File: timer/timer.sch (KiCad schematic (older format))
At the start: 31 parts, among them P1 Keypad, P2 Display, P3 Handset, P4 PWR, P5 Hook, P6 Encoder, P7 SPKR, Q1 S8050, Q2 PN2222A, U1 74HC595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

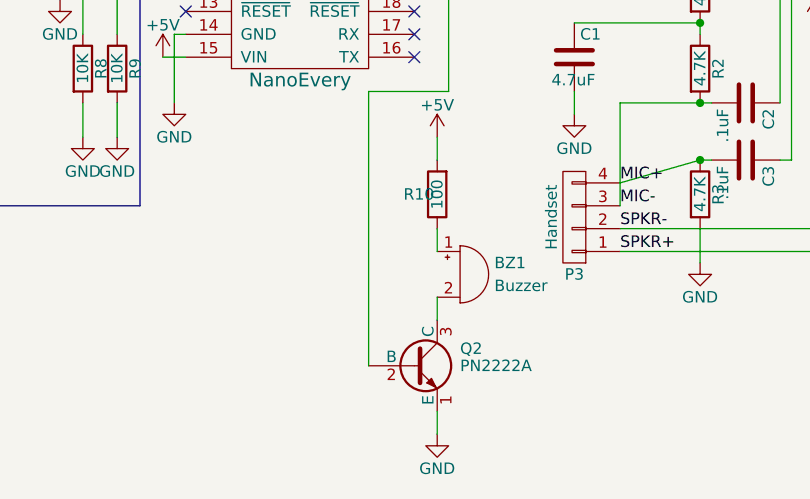
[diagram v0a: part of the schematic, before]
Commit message: added diode D1 to schematic, fixed bug with digitalRead
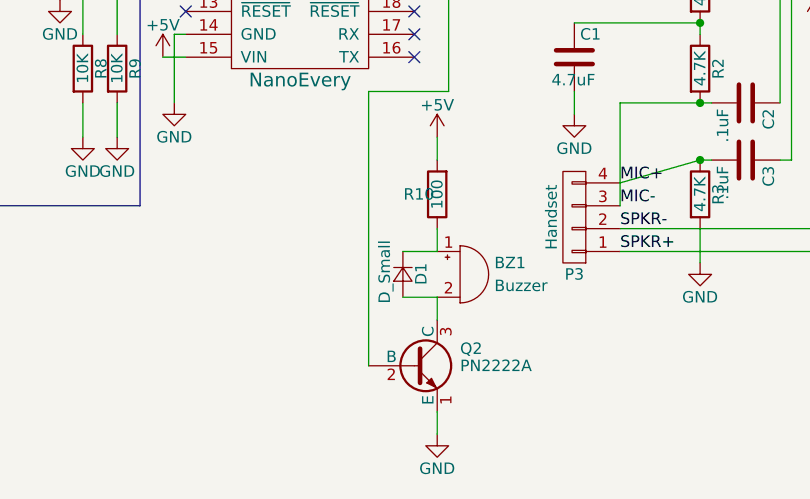
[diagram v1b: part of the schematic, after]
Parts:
- added D1: D_Small, symbol D_Small
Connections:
- net at BZ1.1 (-), R10.1: now also D1.1 (K)
- net at BZ1.2 (+), Q2.3 (C): now also D1.2 (A)
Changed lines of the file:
@@
 $EndComp
 $Comp
-L GND #PWR01
+L GND #PWR2
 U 1 1 5E1F1F7E
 P 3050 2500
-F 0 "#PWR01" H 3050 2250 50  0001 C CNN
+F 0 "#PWR2" H 3050 2250 50  0001 C CNN
 F 1 "GND" H 3050 2350 50  0000 C CNN
 F 2 "" H 3050 2500 50  0000 C CNN
@@
 $EndComp
 $Comp
-L +5V #PWR02
+L +5V #PWR1
 U 1 1 5E1F2C3E
 P 3050 2050
-F 0 "#PWR02" H 3050 1900 50  0001 C CNN
+F 0 "#PWR1" H 3050 1900 50  0001 C CNN
 F 1 "+5V" H 3050 2190 50  0000 C CNN
 F 2 "" H 3050 2050 50  0000 C CNN
@@
 $EndComp
 $Comp
-L GND #PWR03
+L GND #PWR28
 U 1 1 5E1FC8DD
 P 9300 3600
-F 0 "#PWR03" H 9300 3350 50  0001 C CNN
+F 0 "#PWR28" H 9300 3350 50  0001 C CNN
 F 1 "GND" H 9300 3450 50  0000 C CNN
 F 2 "" H 9300 3600 50  0000 C CNN
@@
 $EndComp
 $Comp
-L +5V #PWR04
+L +5V #PWR25
 U 1 1 5E1FC95C
 P 7900 2600
-F 0 "#PWR04" H 7900 2450 50  0001 C CNN
+F 0 "#PWR25" H 7900 2450 50  0001 C CNN
 F 1 "+5V" H 7900 2740 50  0000 C CNN
 F 2 "" H 7900 2600 50  0000 C CNN
@@
 $EndComp
 $Comp
-L +5V #PWR05
+L +5V #PWR23
 U 1 1 5E1FC9C9
 P 7500 4050
-F 0 "#PWR05" H 7500 3900 50  0001 C CNN
+F 0 "#PWR23" H 7500 3900 50  0001 C CNN
 F 1 "+5V" H 7500 4190 50  0000 C CNN
 F 2 "" H 7500 4050 50  0000 C CNN
@@
 $EndComp
 $Comp
-L GND #PWR06
+L GND #PWR26
 U 1 1 5E1FCA32
 P 7900 4500
-F 0 "#PWR06" H 7900 4250 50  0001 C CNN
+F 0 "#PWR26" H 7900 4250 50  0001 C CNN
 F 1 "GND" H 7900 4350 50  0000 C CNN
 F 2 "" H 7900 4500 50  0000 C CNN
@@
 $EndComp
 $Comp
-L GND #PWR07
+L GND #PWR24
 U 1 1 5E1FCA50
 P 7700 4400
-F 0 "#PWR07" H 7700 4150 50  0001 C CNN
+F 0 "#PWR24" H 7700 4150 50  0001 C CNN
 F 1 "GND" H 7700 4250 50  0000 C CNN
 F 2 "" H 7700 4400 50  0000 C CNN
@@
 $EndComp
 $Comp
-L GND #PWR08
+L GND #PWR30
 U 1 1 5E1FCA6E
 P 9350 4000
-F 0 "#PWR08" H 9350 3750 50  0001 C CNN
+F 0 "#PWR30" H 9350 3750 50  0001 C CNN
 F 1 "GND" H 9350 3850 50  0000 C CNN
 F 2 "" H 9350 4000 50  0000 C CNN
@@
 $EndComp
 $Comp
-L GND #PWR09
+L GND #PWR29
 U 1 1 5E1FCA8C
 P 9350 2800
-F 0 "#PWR09" H 9350 2550 50  0001 C CNN
+F 0 "#PWR29" H 9350 2550 50  0001 C CNN
 F 1 "GND" H 9350 2650 50  0000 C CNN
 F 2 "" H 9350 2800 50  0000 C CNN
@@
 $EndComp
 $Comp
-L GND #PWR010
+L GND #PWR22
 U 1 1 5E21BE44
 P 7500 2900
-F 0 "#PWR010" H 7500 2650 50  0001 C CNN
+F 0 "#PWR22" H 7500 2650 50  0001 C CNN
 F 1 "GND" H 7500 2750 50  0000 C CNN
 F 2 "" H 7500 2900 50  0000 C CNN
@@
 $EndComp
 $Comp
-L GND #PWR011
+L GND #PWR31
 U 1 1 5E21C2BB
 P 9600 3500
-F 0 "#PWR011" H 9600 3250 50  0001 C CNN
+F 0 "#PWR31" H 9600 3250 50  0001 C CNN
 F 1 "GND" H 9600 3350 50  0000 C CNN
 F 2 "" H 9600 3500 50  0000 C CNN
@@
 $EndComp
 $Comp
-L GND #PWR012
+L GND #PWR32
 U 1 1 5E21C486
 P 9750 3850
-F 0 "#PWR012" H 9750 3600 50  0001 C CNN
+F 0 "#PWR32" H 9750 3600 50  0001 C CNN
 F 1 "GND" H 9750 3700 50  0000 C CNN
 F 2 "" H 9750 3850 50  0000 C CNN
@@
 $EndComp
 $Comp
-L +5V #PWR013
+L +5V #PWR27
 U 1 1 5E254DF9
 P 9150 3450
-F 0 "#PWR013" H 9150 3300 50  0001 C CNN
+F 0 "#PWR27" H 9150 3300 50  0001 C CNN
 F 1 "+5V" H 9150 3590 50  0000 C CNN
 F 2 "" H 9150 3450 50  0000 C CNN
@@
 $EndComp
 $Comp
-L +5V #PWR014
+L +5V #PWR20
 U 1 1 5E255EBE
 P 7000 3650
-F 0 "#PWR014" H 7000 3500 50  0001 C CNN
+F 0 "#PWR20" H 7000 3500 50  0001 C CNN
 F 1 "+5V" H 7000 3790 50  0000 C CNN
 F 2 "" H 7000 3650 50  0000 C CNN
@@
 $EndComp
 $Comp
-L GND #PWR015
+L GND #PWR21
 U 1 1 5E255FFF
 P 7000 5100
-F 0 "#PWR015" H 7000 4850 50  0001 C CNN
+F 0 "#PWR21" H 7000 4850 50  0001 C CNN
 F 1 "GND" H 7000 4950 50  0000 C CNN
 F 2 "" H 7000 5100 50  0000 C CNN
@@
 $EndComp
 $Comp
-L GND #PWR016
+L GND #PWR33
 U 1 1 5E257195
 P 9950 4900
-F 0 "#PWR016" H 9950 4650 50  0001 C CNN
+F 0 "#PWR33" H 9950 4650 50  0001 C CNN
 F 1 "GND" H 9950 4750 50  0000 C CNN
 F 2 "" H 9950 4900 50  0000 C CNN
@@
 $EndComp
 $Comp
-L +5V #PWR017
+L +5V #PWR34
 U 1 1 5E257AF2
 P 10300 4150
-F 0 "#PWR017" H 10300 4000 50  0001 C CNN
+F 0 "#PWR34" H 10300 4000 50  0001 C CNN
 F 1 "+5V" H 10300 4290 50  0000 C CNN
 F 2 "" H 10300 4150 50  0000 C CNN
@@
 $EndComp
 $Comp
-L GND #PWR018
+L GND #PWR18
 U 1 1 5E25949D
 P 6450 4450
-F 0 "#PWR018" H 6450 4200 50  0001 C CNN
+F 0 "#PWR18" H 6450 4200 50  0001 C CNN
 F 1 "GND" H 6450 4300 50  0000 C CNN
 F 2 "" H 6450 4450 50  0000 C CNN
@@
 $EndComp
 $Comp
-L +5V #PWR020
+L +5V #PWR15
 U 1 1 5E25EB56
 P 5800 2150
-F 0 "#PWR020" H 5800 2000 50  0001 C CNN
+F 0 "#PWR15" H 5800 2000 50  0001 C CNN
 F 1 "+5V" H 5800 2290 50  0000 C CNN
 F 2 "" H 5800 2150 50  0000 C CNN
@@
 $EndComp
 $Comp
-L GND #PWR021
+L GND #PWR19
 U 1 1 5E25EC43
 P 6600 2150
-F 0 "#PWR021" H 6600 1900 50  0001 C CNN
+F 0 "#PWR19" H 6600 1900 50  0001 C CNN
 F 1 "GND" H 6600 2000 50  0000 C CNN
 F 2 "" H 6600 2150 50  0000 C CNN
@@
 $EndComp
 $Comp
-L +5V #PWR022
+L +5V #PWR11
 U 1 1 5E25F4BB
 P 4650 4200
-F 0 "#PWR022" H 4650 4050 50  0001 C CNN
+F 0 "#PWR11" H 4650 4050 50  0001 C CNN
 F 1 "+5V" H 4650 4340 50  0000 C CNN
 F 2 "" H 4650 4200 50  0000 C CNN
@@
 $EndComp
 $Comp
-L GND #PWR023
+L GND #PWR12
 U 1 1 5E25F508
 P 4700 4400
-F 0 "#PWR023" H 4700 4150 50  0001 C CNN
+F 0 "#PWR12" H 4700 4150 50  0001 C CNN
 F 1 "GND" H 4700 4250 50  0000 C CNN
 F 2 "" H 4700 4400 50  0000 C CNN
@@
 $EndComp
 $Comp
-L GND #PWR024
+L GND #PWR10
 U 1 1 5E25F9A8
 P 4500 2200
-F 0 "#PWR024" H 4500 1950 50  0001 C CNN
+F 0 "#PWR10" H 4500 1950 50  0001 C CNN
 F 1 "GND" H 4500 2050 50  0000 C CNN
 F 2 "" H 4500 2200 50  0000 C CNN
@@
 $EndComp
 $Comp
-L +5V #PWR025
+L +5V #PWR13
 U 1 1 5E25F9F8
 P 4800 2150
-F 0 "#PWR025" H 4800 2000 50  0001 C CNN
+F 0 "#PWR13" H 4800 2000 50  0001 C CNN
 F 1 "+5V" H 4800 2290 50  0000 C CNN
 F 2 "" H 4800 2150 50  0000 C CNN
@@
 	6300 3300 6300 2150
 $Comp
-L GND #PWR026
+L GND #PWR5
 U 1 1 5E260E32
 P 3850 3350
-F 0 "#PWR026" H 3850 3100 50  0001 C CNN
+F 0 "#PWR5" H 3850 3100 50  0001 C CNN
 F 1 "GND" H 3850 3200 50  0000 C CNN
 F 2 "" H 3850 3350 50  0000 C CNN
@@
 NoConn ~ 7900 2900
 $Comp
-L +5V #PWR027
+L +5V #PWR3
 U 1 1 5E27D47A
 P 3200 4200
-F 0 "#PWR027" H 3200 4050 50  0001 C CNN
+F 0 "#PWR3" H 3200 4050 50  0001 C CNN
 F 1 "+5V" H 3200 4340 50  0000 C CNN
 F 2 "" H 3200 4200 50  0000 C CNN
@@
 	3000 4200 3000 4050
 $Comp
-L GND #PWR028
+L GND #PWR4
 U 1 1 5E27DD28
 P 3550 2900
-F 0 "#PWR028" H 3550 2650 50  0001 C CNN
+F 0 "#PWR4" H 3550 2650 50  0001 C CNN
 F 1 "GND" H 3550 2750 50  0000 C CNN
 F 2 "" H 3550 2900 50  0000 C CNN
@@
 	4200 3400 4200 3500
 $Comp
-L GND #PWR029
+L GND #PWR6
 U 1 1 5E2CB89E
 P 4050 3750
-F 0 "#PWR029" H 4050 3500 50  0001 C CNN
+F 0 "#PWR6" H 4050 3500 50  0001 C CNN
 F 1 "GND" H 4050 3600 50  0000 C CNN
 F 2 "" H 4050 3750 50  0000 C CNN
@@
 $EndComp
 $Comp
-L GND #PWR030
+L GND #PWR7
 U 1 1 5E2CB900
 P 4200 3950
-F 0 "#PWR030" H 4200 3700 50  0001 C CNN
+F 0 "#PWR7" H 4200 3700 50  0001 C CNN
 F 1 "GND" H 4200 3800 50  0000 C CNN
 F 2 "" H 4200 3950 50  0000 C CNN
@@
 $EndComp
 $Comp
-L GND #PWR031
+L GND #PWR8
 U 1 1 5E2CB962
 P 4300 4550
-F 0 "#PWR031" H 4300 4300 50  0001 C CNN
+F 0 "#PWR8" H 4300 4300 50  0001 C CNN
 F 1 "GND" H 4300 4400 50  0000 C CNN
 F 2 "" H 4300 4550 50  0000 C CNN
@@
 $EndComp
 $Comp
-L GND #PWR032
+L GND #PWR9
 U 1 1 5E2CB9C4
 P 4450 4550
-F 0 "#PWR032" H 4450 4300 50  0001 C CNN
+F 0 "#PWR9" H 4450 4300 50  0001 C CNN
 F 1 "GND" H 4450 4400 50  0000 C CNN
 F 2 "" H 4450 4550 50  0000 C CNN
@@
 $EndComp
 $Comp
-L GND #PWR033
+L GND #PWR17
 U 1 1 5E31038E
 P 5850 5850
-F 0 "#PWR033" H 5850 5600 50  0001 C CNN
+F 0 "#PWR17" H 5850 5600 50  0001 C CNN
 F 1 "GND" H 5850 5700 50  0000 C CNN
 F 2 "" H 5850 5850 50  0000 C CNN
@@
 $EndComp
 $Comp
-L +5V #PWR034
+L +5V #PWR16
 U 1 1 5E31063C
 P 5850 4550
-F 0 "#PWR034" H 5850 4400 50  0001 C CNN
+F 0 "#PWR16" H 5850 4400 50  0001 C CNN
 F 1 "+5V" H 5850 4690 50  0000 C CNN
 F 2 "" H 5850 4550 50  0000 C CNN
@@
 	5800 2150 6100 2150
 $Comp
-L GND #PWR?
+L GND #PWR14
 U 1 1 5E66D489
 P 5400 2150
-F 0 "#PWR?" H 5400 1900 50  0001 C CNN
+F 0 "#PWR14" H 5400 1900 50  0001 C CNN
 F 1 "GND" H 5400 2000 50  0000 C CNN
 F 2 "" H 5400 2150 50  0000 C CNN
@@
 	1    0    0    -1
 $EndComp
+$Comp
+L D_Small D1
+U 1 1 5EC37F50
+P 5700 5150
+F 0 "D1" H 5650 5230 50  0000 L CNN
+F 1 "D_Small" H 5550 5070 50  0000 L CNN
+F 2 "" V 5700 5150 50  0000 C CNN
+F 3 "" V 5700 5150 50  0000 C CNN
+	1    5700 5150
+	0    1    1    0
+$EndComp
+Wire Wire Line
+	5850 5050 5700 5050
+Wire Wire Line
+	5700 5250 5850 5250
 $EndSCHEMATC

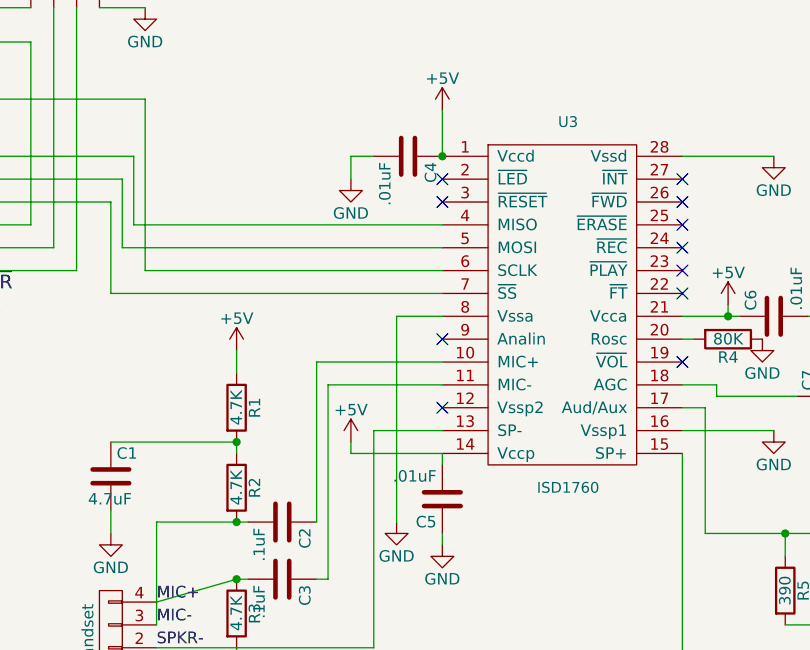
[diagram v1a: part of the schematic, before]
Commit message: Change capacater value
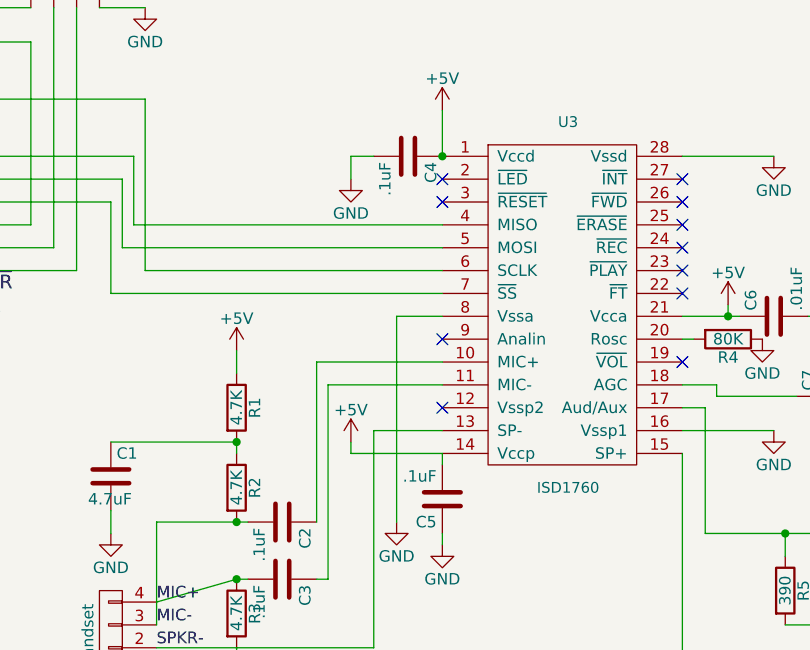
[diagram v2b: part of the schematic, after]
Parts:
- C4, C5: value .01uF -> .1uF
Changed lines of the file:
@@
 P 7750 2800
 F 0 "C4" H 7775 2900 50  0000 L CNN
-F 1 ".01uF" H 7775 2700 50  0000 L CNN
+F 1 ".1uF" H 7775 2700 50  0000 L CNN
 F 2 "" H 7788 2650 50  0000 C CNN
 F 3 "" H 7750 2800 50  0000 C CNN
@@
 P 7900 4300
 F 0 "C5" H 7925 4400 50  0000 L CNN
-F 1 ".01uF" H 7925 4200 50  0000 L CNN
+F 1 ".1uF" H 7925 4200 50  0000 L CNN
 F 2 "" H 7938 4150 50  0000 C CNN
 F 3 "" H 7900 4300 50  0000 C CNN

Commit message: timer changes
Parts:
- BZ1: symbol Buzzer -> Device:Buzzer
- C1, C2, C3, C4, C5, C6, C7, C8: symbol C -> Device:C
- D1: symbol D_Small -> Device:D_Small
- P1: symbol CONN_01X14 -> timer-rescue:CONN_01X14
- P2, P3, P6: symbol CONN_01X04 -> timer-rescue:CONN_01X04
- P4, P5, P7: symbol CONN_01X02 -> timer-rescue:CONN_01X02
- Q1: symbol S8050 -> timer-rescue:S8050
- Q2: symbol PN2222A -> timer-rescue:PN2222A
- R1, R10, R2, R3, R4, R5, R6, R7, R8, R9: symbol R -> Device:R
- U1: symbol 74HC595 -> timer-rescue:74HC595
- U2: symbol NanoEvery -> timer:NanoEvery
- U3: symbol ISD1740 -> timer:ISD1740
